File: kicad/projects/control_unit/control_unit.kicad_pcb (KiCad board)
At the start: 2 copper layers, 165.1 x 50.8 mm, 4 parts, among them U1 28C256, U2 28C256, U3 28C256, U4 28C256

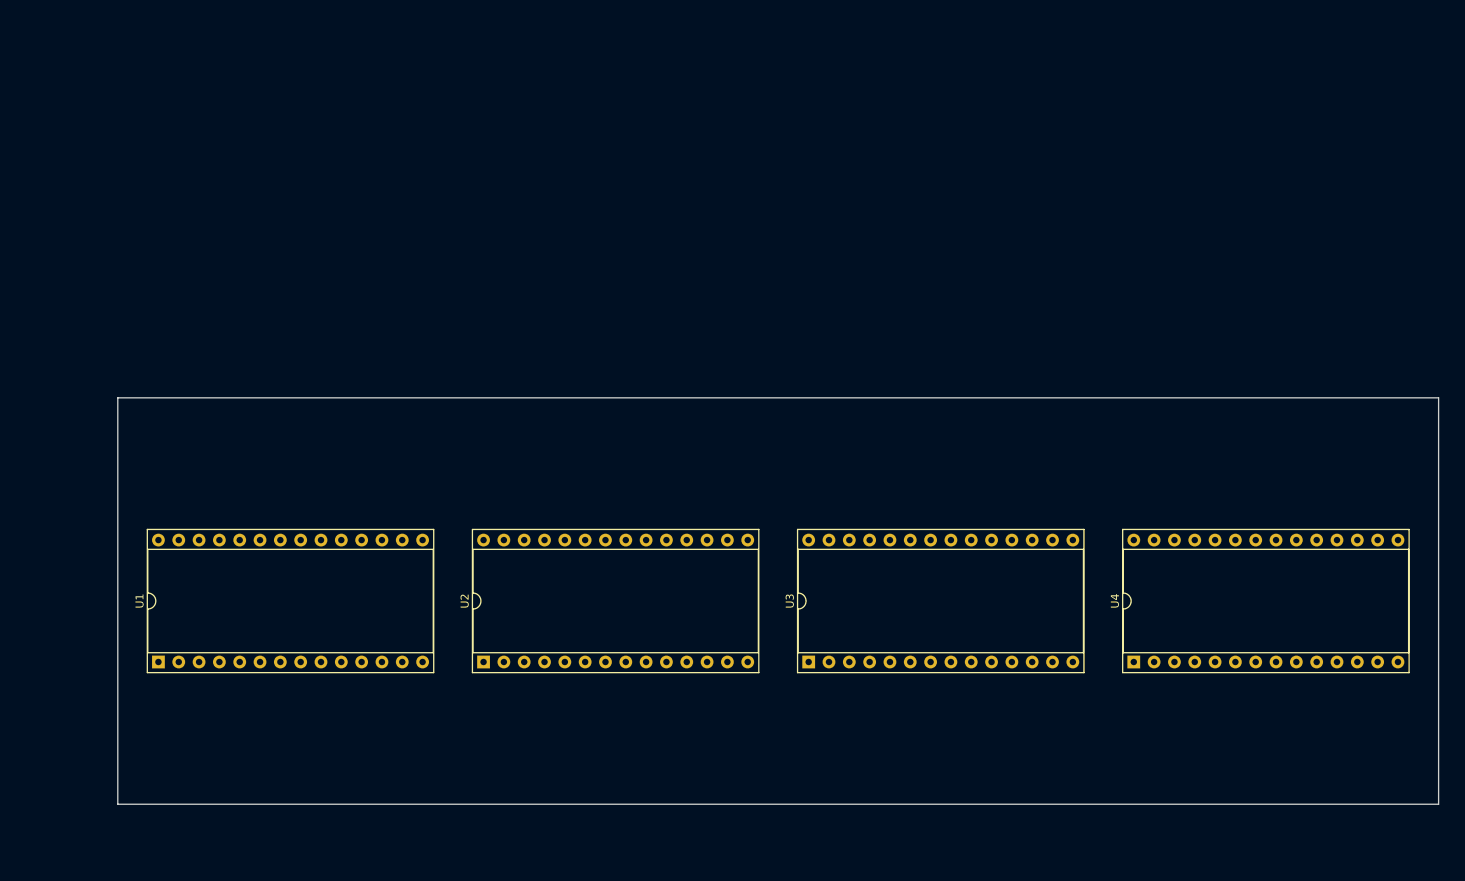
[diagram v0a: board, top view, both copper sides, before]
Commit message: Start control unit - make board slightly larger to accomodate control unit and ALU needs.
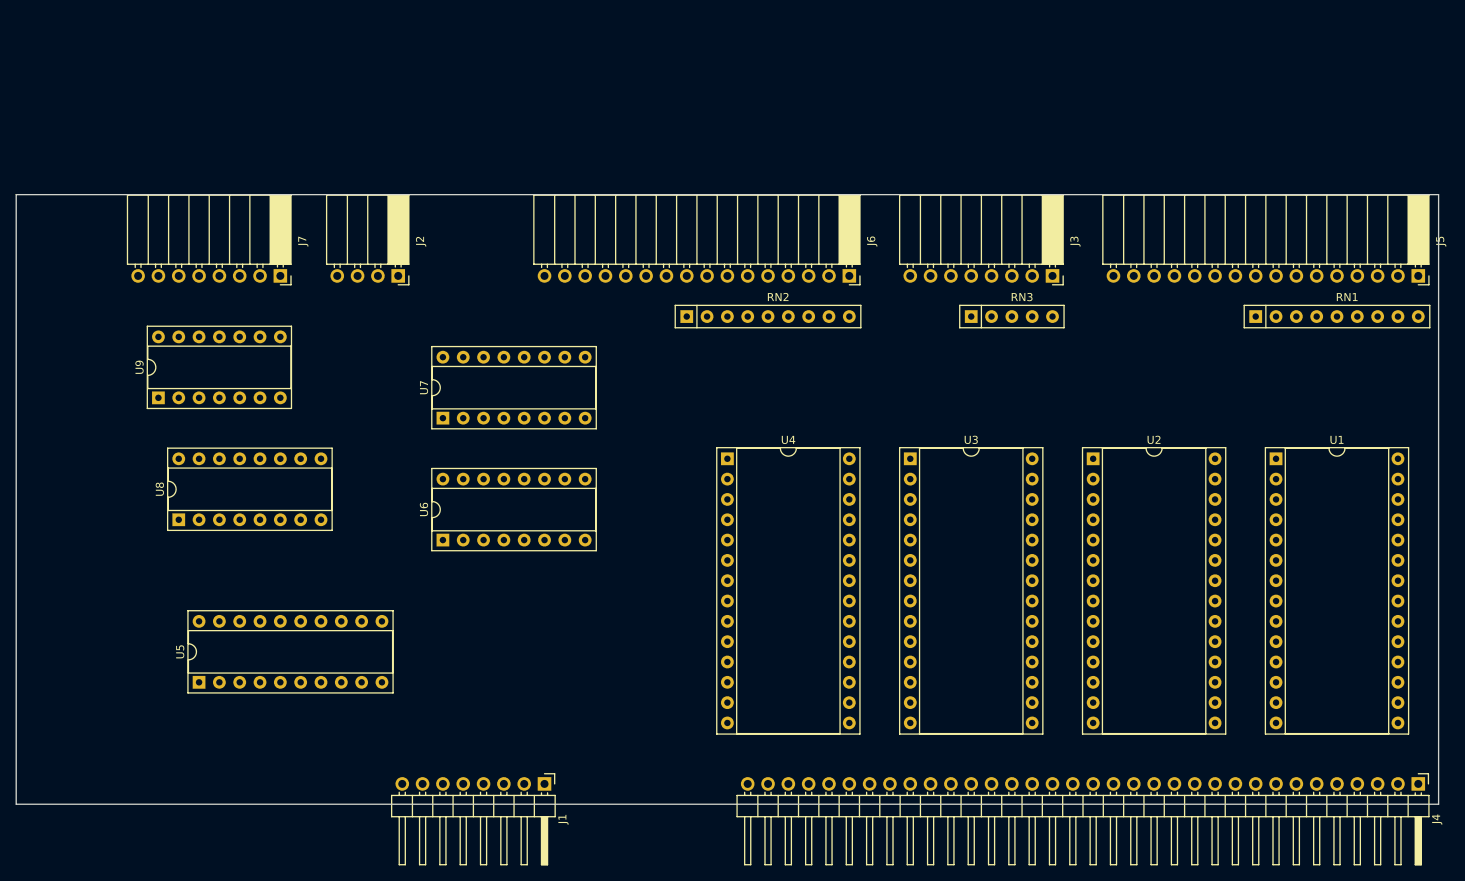
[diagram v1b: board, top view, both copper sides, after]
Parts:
- added J1: Conn_01x08_Male, Connector_PinHeader_2.54mm:PinHeader_1x08_P2.54mm_Horizontal, F.Cu at (111.8, 116.8)
- added J2: Conn_01x04_Female, Connector_PinSocket_2.54mm:PinSocket_1x04_P2.54mm_Horizontal, F.Cu at (93.5, 53.3)
- added J3: Conn_01x08_Female, Connector_PinSocket_2.54mm:PinSocket_1x08_P2.54mm_Horizontal, F.Cu at (175.3, 53.3)
- added J4: Conn_01x34_Male, Connector_PinHeader_2.54mm:PinHeader_1x34_P2.54mm_Horizontal, F.Cu at (221.0, 116.8)
- added J5: Conn_01x16_Female, Connector_PinSocket_2.54mm:PinSocket_1x16_P2.54mm_Horizontal, F.Cu at (221.0, 53.3)
- added J6: Conn_01x16_Female, Connector_PinSocket_2.54mm:PinSocket_1x16_P2.54mm_Horizontal, F.Cu at (149.9, 53.3)
- added J7: Conn_01x08_Female, Connector_PinSocket_2.54mm:PinSocket_1x08_P2.54mm_Horizontal, F.Cu at (78.7, 53.3)
- added RN1: R_Network08_US, Resistor_THT:R_Array_SIP9, F.Cu at (200.7, 58.4)
- added RN2: R_Network08_US, Resistor_THT:R_Array_SIP9, F.Cu at (129.5, 58.4)
- added RN3: R_Network04_US, Resistor_THT:R_Array_SIP5, F.Cu at (165.1, 58.4)
- added U5: 74HCT377, Package_DIP:DIP-20_W7.62mm_Socket, F.Cu at (68.6, 104.1)
- added U6: 74HCT161, Package_DIP:DIP-16_W7.62mm_Socket, F.Cu at (99.1, 86.4)
- added U7: 74HCT173, Package_DIP:DIP-16_W7.62mm_Socket, F.Cu at (99.1, 71.1)
- added U8: 74HCT138, Package_DIP:DIP-16_W7.62mm_Socket, F.Cu at (66.0, 83.8)
- added U9: 74HCT04, Package_DIP:DIP-14_W7.62mm_Socket, F.Cu at (63.5, 68.6)
- moved U1 142.0 mm to (203.2, 76.2), turned to 0 degrees
- moved U2 80.3 mm to (180.3, 76.2), turned to 0 degrees
- moved U4 56.8 mm to (134.6, 76.2), turned to 0 degrees
- moved U3 28.4 mm to (157.5, 76.2), turned to 0 degrees
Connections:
- U1 pad 1: Net-(U1-Pad1) -> /MIR_INST_7
- U1 pad 10: Net-(U1-Pad10) -> /MC_STEP_0
- U1 pad 11: Net-(U1-Pad11) -> /ROM_0_0
- U1 pad 12: Net-(U1-Pad12) -> /ROM_0_1
- U1 pad 13: Net-(U1-Pad13) -> /ROM_0_2
- U1 pad 15: Net-(U1-Pad15) -> /ROM_0_3
- U1 pad 16: Net-(U1-Pad16) -> /ROM_0_4
- U1 pad 17: Net-(U1-Pad17) -> /ROM_0_5
- U1 pad 18: Net-(U1-Pad18) -> /ROM_0_6
- U1 pad 19: Net-(U1-Pad19) -> /ROM_0_7
- U1 pad 2: Net-(U1-Pad2) -> /MIR_INST_5
- U1 pad 21: Net-(U1-Pad21) -> /MIR_INST_3
- U1 pad 23: Net-(U1-Pad23) -> /MIR_INST_4
- U1 pad 24: Net-(U1-Pad24) -> /MIR_INST_2
- U1 pad 25: Net-(U1-Pad25) -> /MIR_INST_1
- U1 pad 26: Net-(U1-Pad26) -> /MIR_INST_6
- U1 pad 3: Net-(U1-Pad3) -> /MIR_INST_0
- U1 pad 4: Net-(U1-Pad4) -> /MIR_FLAG_E
- U1 pad 5: Net-(U1-Pad5) -> /MIR_FLAG_C
- U1 pad 6: Net-(U1-Pad6) -> /MIR_FLAG_N
- U1 pad 7: Net-(U1-Pad7) -> /MIR_FLAG_Z
- U1 pad 8: Net-(U1-Pad8) -> /MC_STEP_2
- U1 pad 9: Net-(U1-Pad9) -> /MC_STEP_1
- U2 pad 1: Net-(U2-Pad1) -> /MIR_INST_7
- U2 pad 10: Net-(U2-Pad10) -> /MC_STEP_0
- U2 pad 11: Net-(U2-Pad11) -> /ROM_1_0
- U2 pad 12: Net-(U2-Pad12) -> /ROM_1_1
- U2 pad 13: Net-(U2-Pad13) -> /ROM_1_2
- U2 pad 15: Net-(U2-Pad15) -> /ROM_1_3
- U2 pad 16: Net-(U2-Pad16) -> /ROM_1_4
- U2 pad 17: Net-(U2-Pad17) -> /ROM_1_5
- U2 pad 18: Net-(U2-Pad18) -> /ROM_1_6
- U2 pad 19: Net-(U2-Pad19) -> /ROM_1_7
- U2 pad 2: Net-(U2-Pad2) -> /MIR_INST_5
- U2 pad 21: Net-(U2-Pad21) -> /MIR_INST_3
- U2 pad 23: Net-(U2-Pad23) -> /MIR_INST_4
- U2 pad 24: Net-(U2-Pad24) -> /MIR_INST_2
- U2 pad 25: Net-(U2-Pad25) -> /MIR_INST_1
- U2 pad 26: Net-(U2-Pad26) -> /MIR_INST_6
- U2 pad 3: Net-(U2-Pad3) -> /MIR_INST_0
- U2 pad 4: Net-(U2-Pad4) -> /MIR_FLAG_E
- U2 pad 5: Net-(U2-Pad5) -> /MIR_FLAG_C
- U2 pad 6: Net-(U2-Pad6) -> /MIR_FLAG_N
- U2 pad 7: Net-(U2-Pad7) -> /MIR_FLAG_Z
- U2 pad 8: Net-(U2-Pad8) -> /MC_STEP_2
- U2 pad 9: Net-(U2-Pad9) -> /MC_STEP_1
- U3 pad 1: Net-(U3-Pad1) -> /MIR_INST_7
- U3 pad 10: Net-(U3-Pad10) -> /MC_STEP_0
- U3 pad 11: Net-(U3-Pad11) -> /ROM_2_0
- U3 pad 12: Net-(U3-Pad12) -> /ROM_2_1
- U3 pad 13: Net-(U3-Pad13) -> /ROM_2_2
- U3 pad 15: Net-(U3-Pad15) -> /ROM_2_3
- U3 pad 16: Net-(U3-Pad16) -> /ROM_2_4
- U3 pad 17: Net-(U3-Pad17) -> /ROM_2_5
- U3 pad 18: Net-(U3-Pad18) -> /ROM_2_6
- U3 pad 19: Net-(U3-Pad19) -> /ROM_2_7
- U3 pad 2: Net-(U3-Pad2) -> /MIR_INST_5
- U3 pad 21: Net-(U3-Pad21) -> /MIR_INST_3
- U3 pad 23: Net-(U3-Pad23) -> /MIR_INST_4
- U3 pad 24: Net-(U3-Pad24) -> /MIR_INST_2
- U3 pad 25: Net-(U3-Pad25) -> /MIR_INST_1
- U3 pad 26: Net-(U3-Pad26) -> /MIR_INST_6
- U3 pad 3: Net-(U3-Pad3) -> /MIR_INST_0
- U3 pad 4: Net-(U3-Pad4) -> /MIR_FLAG_E
- U3 pad 5: Net-(U3-Pad5) -> /MIR_FLAG_C
- U3 pad 6: Net-(U3-Pad6) -> /MIR_FLAG_N
- U3 pad 7: Net-(U3-Pad7) -> /MIR_FLAG_Z
- U3 pad 8: Net-(U3-Pad8) -> /MC_STEP_2
- U3 pad 9: Net-(U3-Pad9) -> /MC_STEP_1
- U4 pad 1: Net-(U4-Pad1) -> /MIR_INST_7
- U4 pad 10: Net-(U4-Pad10) -> /MC_STEP_0
- U4 pad 11: Net-(U4-Pad11) -> /ROM_3_0
- U4 pad 12: Net-(U4-Pad12) -> /ROM_3_1
- U4 pad 13: Net-(U4-Pad13) -> /ROM_3_2
- U4 pad 15: Net-(U4-Pad15) -> /ROM_3_3
- U4 pad 16: Net-(U4-Pad16) -> /ROM_3_4
- U4 pad 17: Net-(U4-Pad17) -> /ROM_3_5
- U4 pad 18: Net-(U4-Pad18) -> /ROM_3_6
- U4 pad 19: Net-(U4-Pad19) -> /ROM_3_7
- U4 pad 2: Net-(U4-Pad2) -> /MIR_INST_5
- U4 pad 21: Net-(U4-Pad21) -> /MIR_INST_3
- U4 pad 23: Net-(U4-Pad23) -> /MIR_INST_4
- U4 pad 24: Net-(U4-Pad24) -> /MIR_INST_2
- U4 pad 25: Net-(U4-Pad25) -> /MIR_INST_1
- U4 pad 26: Net-(U4-Pad26) -> /MIR_INST_6
- U4 pad 3: Net-(U4-Pad3) -> /MIR_INST_0
- U4 pad 4: Net-(U4-Pad4) -> /MIR_FLAG_E
- U4 pad 5: Net-(U4-Pad5) -> /MIR_FLAG_C
- U4 pad 6: Net-(U4-Pad6) -> /MIR_FLAG_N
- U4 pad 7: Net-(U4-Pad7) -> /MIR_FLAG_Z
- U4 pad 8: Net-(U4-Pad8) -> /MC_STEP_2
- U4 pad 9: Net-(U4-Pad9) -> /MC_STEP_1
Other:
- board size 165.1 x 50.8 mm -> 177.8 x 76.2 mm

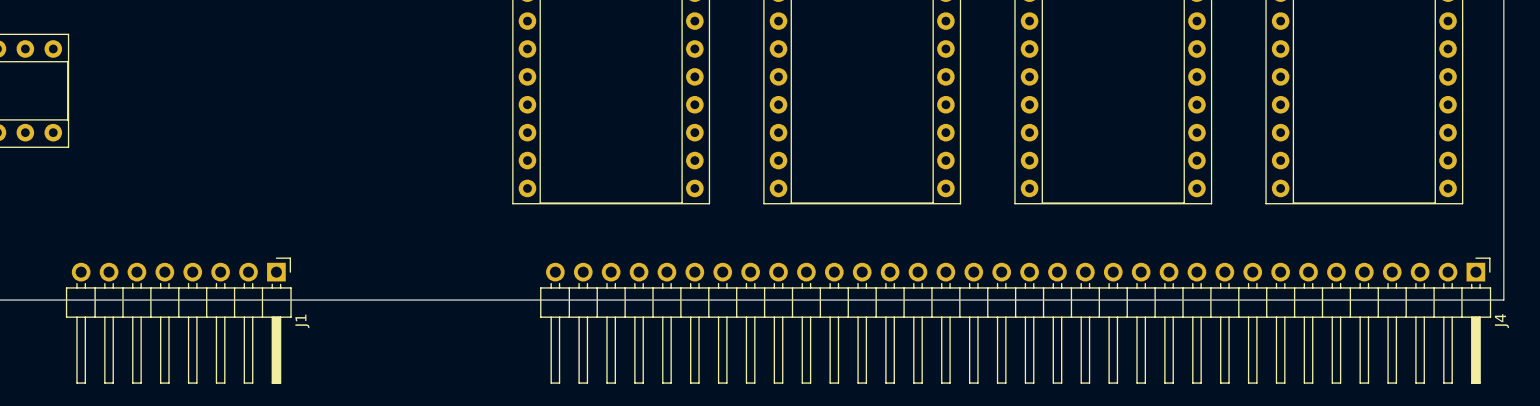
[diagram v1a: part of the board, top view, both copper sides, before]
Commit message: More work on control unit schematic.
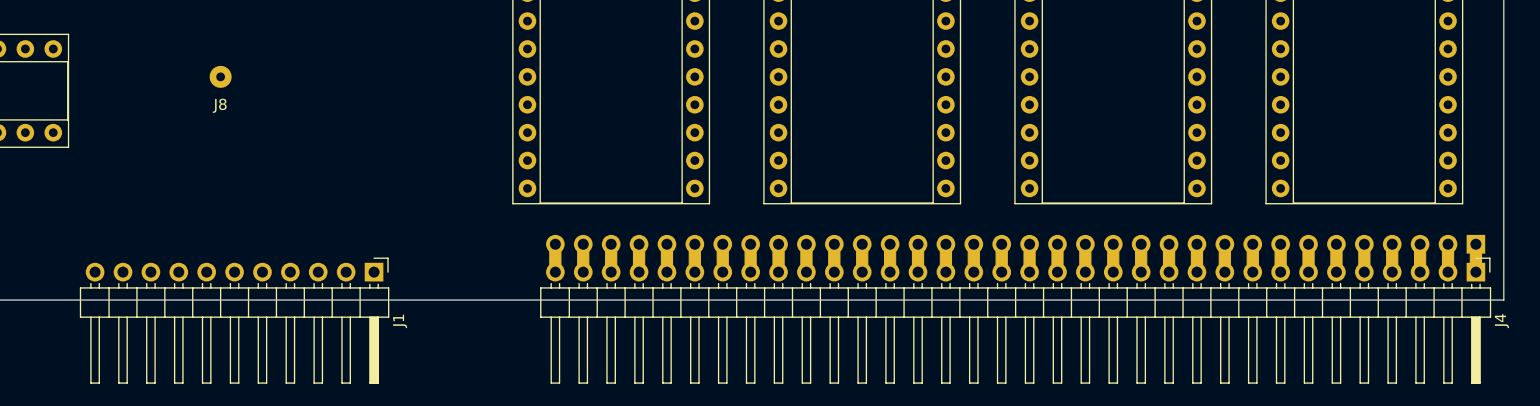
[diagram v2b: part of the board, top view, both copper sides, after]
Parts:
- added J8: Conn_01x01_Female, Connector_Wire:SolderWirePad_1x01_Drill0.8mm, F.Cu at (106.7, 99.1)
- J1: value Conn_01x08_Male -> Conn_01x11_Male; footprint Connector_PinHeader_2.54mm:PinHeader_1x08_P2.54mm_Horizontal -> Connector_PinHeader_2.54mm:PinHeader_1x11_P2.54mm_Horizontal
- J4: footprint Connector_PinHeader_2.54mm:PinHeader_1x34_P2.54mm_Horizontal -> eight-bit-computer:backplane-connector
- moved J1 8.89 mm to (120.7, 116.8)
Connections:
- J4 pad 34: Net-(J4-Pad34) -> /CONTROL_CLOCK
- J5 pad 1: Net-(J5-Pad1) -> /MIR_INST_0
- J5 pad 11: Net-(J5-Pad11) -> /MIR_INST_5
- J5 pad 13: Net-(J5-Pad13) -> /MIR_INST_6
- J5 pad 15: Net-(J5-Pad15) -> /MIR_INST_7
- J5 pad 3: Net-(J5-Pad3) -> /MIR_INST_1
- J5 pad 5: Net-(J5-Pad5) -> /MIR_INST_2
- J5 pad 7: Net-(J5-Pad7) -> /MIR_INST_3
- J5 pad 9: Net-(J5-Pad9) -> /MIR_INST_4
- J7 pad 1: Net-(J7-Pad1) -> /MIR_FLAG_Z
- J7 pad 3: Net-(J7-Pad3) -> /MIR_FLAG_N
- J7 pad 5: Net-(J7-Pad5) -> /MIR_FLAG_C
- J7 pad 7: Net-(J7-Pad7) -> /MIR_FLAG_E
- RN1 pad 2: Net-(RN1-Pad2) -> Net-(J5-Pad2)
- RN1 pad 3: Net-(RN1-Pad3) -> Net-(J5-Pad4)
- RN1 pad 4: Net-(RN1-Pad4) -> Net-(J5-Pad6)
- RN1 pad 5: Net-(RN1-Pad5) -> Net-(J5-Pad8)
- RN1 pad 6: Net-(RN1-Pad6) -> Net-(J5-Pad10)
- RN1 pad 7: Net-(RN1-Pad7) -> Net-(J5-Pad12)
- RN1 pad 8: Net-(RN1-Pad8) -> Net-(J5-Pad14)
- RN1 pad 9: Net-(RN1-Pad9) -> Net-(J5-Pad16)
- RN2 pad 2: Net-(RN2-Pad2) -> Net-(J6-Pad2)
- RN2 pad 3: Net-(RN2-Pad3) -> Net-(J6-Pad4)
- RN2 pad 4: Net-(RN2-Pad4) -> Net-(J6-Pad6)
- RN2 pad 5: Net-(RN2-Pad5) -> Net-(J6-Pad8)
- RN2 pad 6: Net-(RN2-Pad6) -> Net-(J6-Pad10)
- RN2 pad 7: Net-(RN2-Pad7) -> Net-(J6-Pad12)
- RN2 pad 8: Net-(RN2-Pad8) -> Net-(J6-Pad14)
- RN2 pad 9: Net-(RN2-Pad9) -> Net-(J6-Pad16)
- RN3 pad 2: Net-(RN3-Pad2) -> Net-(J7-Pad2)
- RN3 pad 3: Net-(RN3-Pad3) -> Net-(J7-Pad4)
- RN3 pad 4: Net-(RN3-Pad4) -> Net-(J7-Pad6)
- RN3 pad 5: Net-(RN3-Pad5) -> Net-(J7-Pad8)
- U1 pad 14: Net-(U1-Pad14) -> GND
- U2 pad 14: Net-(U2-Pad14) -> GND
- U2 pad 20: Net-(U2-Pad20) -> GND
- U2 pad 22: Net-(U2-Pad22) -> GND
- U3 pad 14: Net-(U3-Pad14) -> GND
- U3 pad 20: Net-(U3-Pad20) -> GND
- U3 pad 22: Net-(U3-Pad22) -> GND
- U4 pad 14: Net-(U4-Pad14) -> GND
- U4 pad 20: Net-(U4-Pad20) -> GND
- U4 pad 22: Net-(U4-Pad22) -> GND
- U5 pad 1: Net-(U5-Pad1) -> GND
- U5 pad 10: Net-(U5-Pad10) -> GND
- U5 pad 11: Net-(U5-Pad11) -> /CONTROL_CLOCK
- U5 pad 13: Net-(U5-Pad13) -> Net-(J3-Pad5)
- U5 pad 14: Net-(U5-Pad14) -> Net-(J3-Pad6)
- U5 pad 17: Net-(U5-Pad17) -> Net-(J3-Pad7)
- U5 pad 18: Net-(U5-Pad18) -> Net-(J3-Pad8)
- U5 pad 3: Net-(U5-Pad3) -> Net-(J3-Pad1)
- U5 pad 4: Net-(U5-Pad4) -> Net-(J3-Pad2)
- U5 pad 7: Net-(U5-Pad7) -> Net-(J3-Pad3)
- U5 pad 8: Net-(U5-Pad8) -> Net-(J3-Pad4)
- U6 pad 10: Net-(U6-Pad10) -> VCC
- U6 pad 2: Net-(U6-Pad2) -> /CONTROL_CLOCK
- U6 pad 3: Net-(U6-Pad3) -> GND
- U6 pad 4: Net-(U6-Pad4) -> GND
- U6 pad 5: Net-(U6-Pad5) -> GND
- U6 pad 6: Net-(U6-Pad6) -> GND
- U6 pad 7: Net-(U6-Pad7) -> VCC
- U7 pad 1: Net-(U7-Pad1) -> GND
- U7 pad 10: Net-(U7-Pad10) -> GND
- U7 pad 11: Net-(U7-Pad11) -> Net-(J2-Pad4)
- U7 pad 12: Net-(U7-Pad12) -> Net-(J2-Pad3)
- U7 pad 13: Net-(U7-Pad13) -> Net-(J2-Pad2)
- U7 pad 14: Net-(U7-Pad14) -> Net-(J2-Pad1)
- U7 pad 15: Net-(U7-Pad15) -> GND
- U7 pad 2: Net-(U7-Pad2) -> GND
- U7 pad 7: Net-(U7-Pad7) -> /CONTROL_CLOCK
- U7 pad 9: Net-(U7-Pad9) -> GND
- U8 pad 1: Net-(U8-Pad1) -> /MC_STEP_0
- U8 pad 10: Net-(U8-Pad10) -> Net-(J6-Pad11)
- U8 pad 11: Net-(U8-Pad11) -> Net-(J6-Pad9)
- U8 pad 12: Net-(U8-Pad12) -> Net-(J6-Pad7)
- U8 pad 13: Net-(U8-Pad13) -> Net-(J6-Pad5)
- U8 pad 14: Net-(U8-Pad14) -> Net-(J6-Pad3)
- U8 pad 15: Net-(U8-Pad15) -> Net-(J6-Pad1)
- U8 pad 2: Net-(U8-Pad2) -> /MC_STEP_1
- U8 pad 3: Net-(U8-Pad3) -> /MC_STEP_2
- U8 pad 7: Net-(U8-Pad7) -> Net-(J6-Pad15)
- U8 pad 9: Net-(U8-Pad9) -> Net-(J6-Pad13)
- U9 pad 1: Net-(U9-Pad1) -> /MASTER_RESET
- U9 pad 2: Net-(U9-Pad2) -> Net-(U6-Pad1)
- U9 pad 4: Net-(U9-Pad4) -> Net-(U6-Pad9)
